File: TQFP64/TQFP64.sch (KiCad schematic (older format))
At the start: 6 parts, among them J1 Conn_01x32, J2 Conn_02x32_Counter_Clockwise, J3 Conn_02x32_Counter_Clockwise, J4 Conn_02x32_Counter_Clockwise, J5 Conn_01x32, J6 Conn_01x06

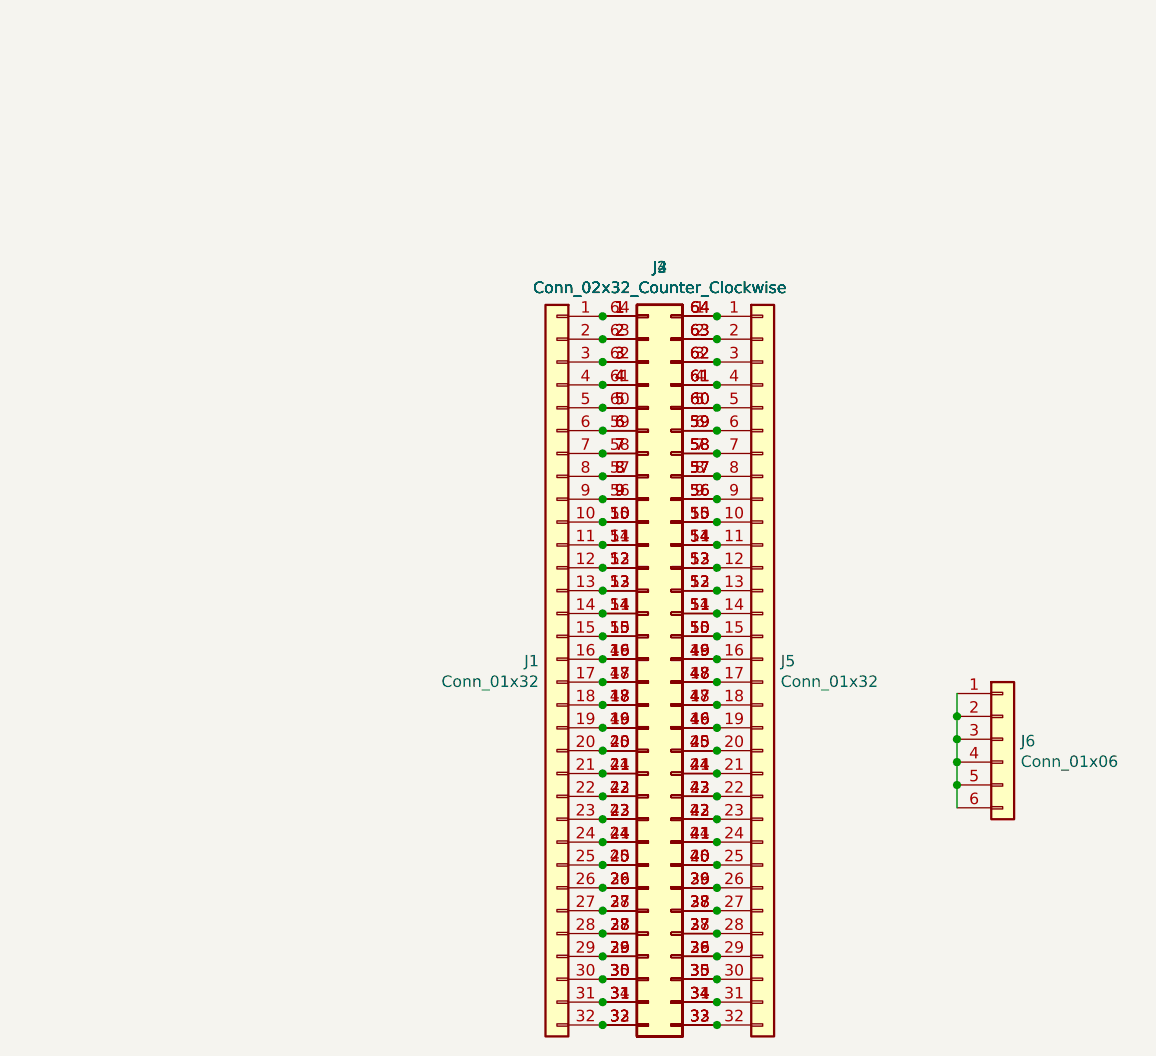
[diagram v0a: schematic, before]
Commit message: USB, SD and CR Cells Added
MicroSD, MicroUSB, MiniUSB, USB-C, CR1220, CR2032 added as well as all schematics page sizes optimised
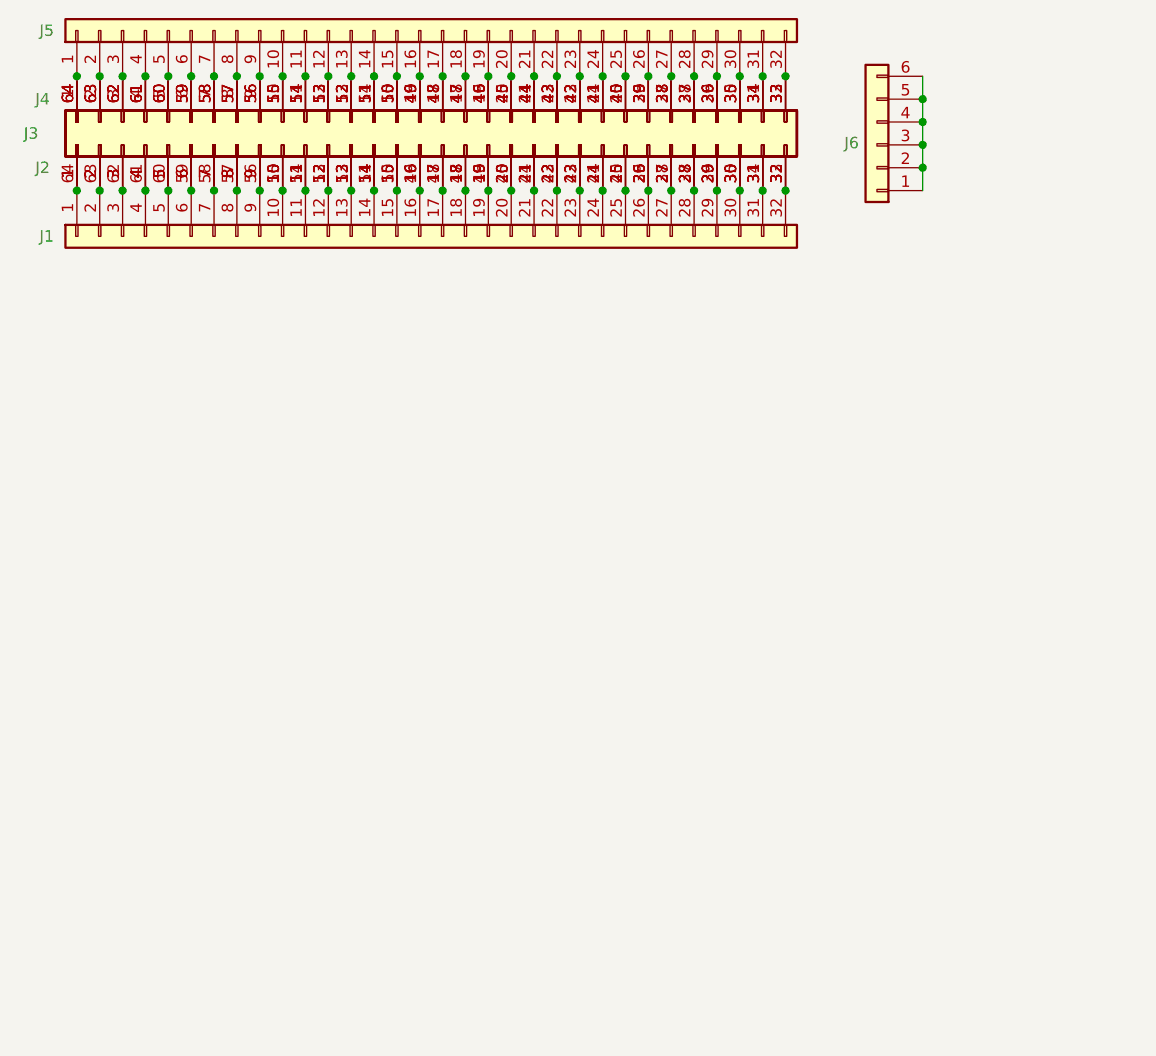
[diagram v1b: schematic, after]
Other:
- moved on the sheet: J1, J2, J3, J4, J5, J6
